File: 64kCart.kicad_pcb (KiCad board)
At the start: 2 copper layers, 9 parts, among them SW1 SW_Push, U1 27C512, U2 74LS173, U3 74LS04, U4 C64-Exp-Port

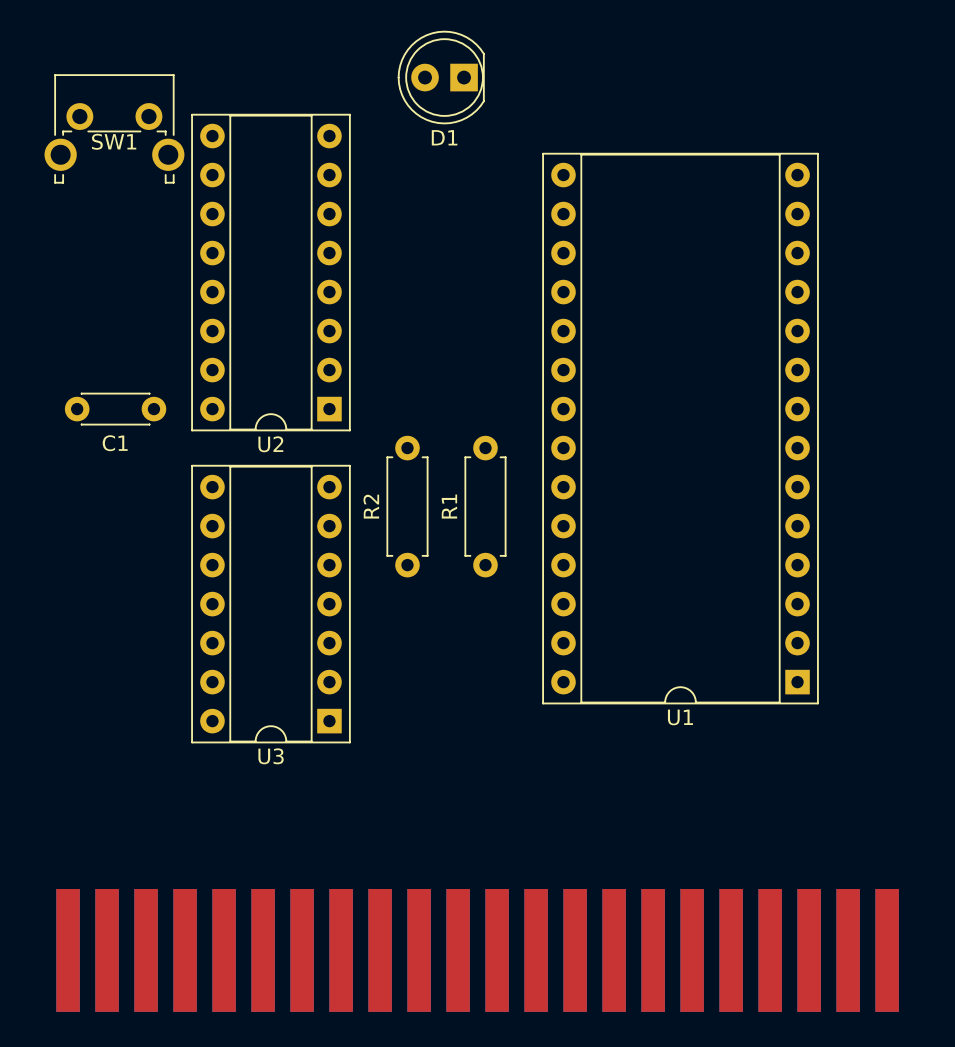
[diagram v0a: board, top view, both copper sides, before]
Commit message: Some work on board layout.
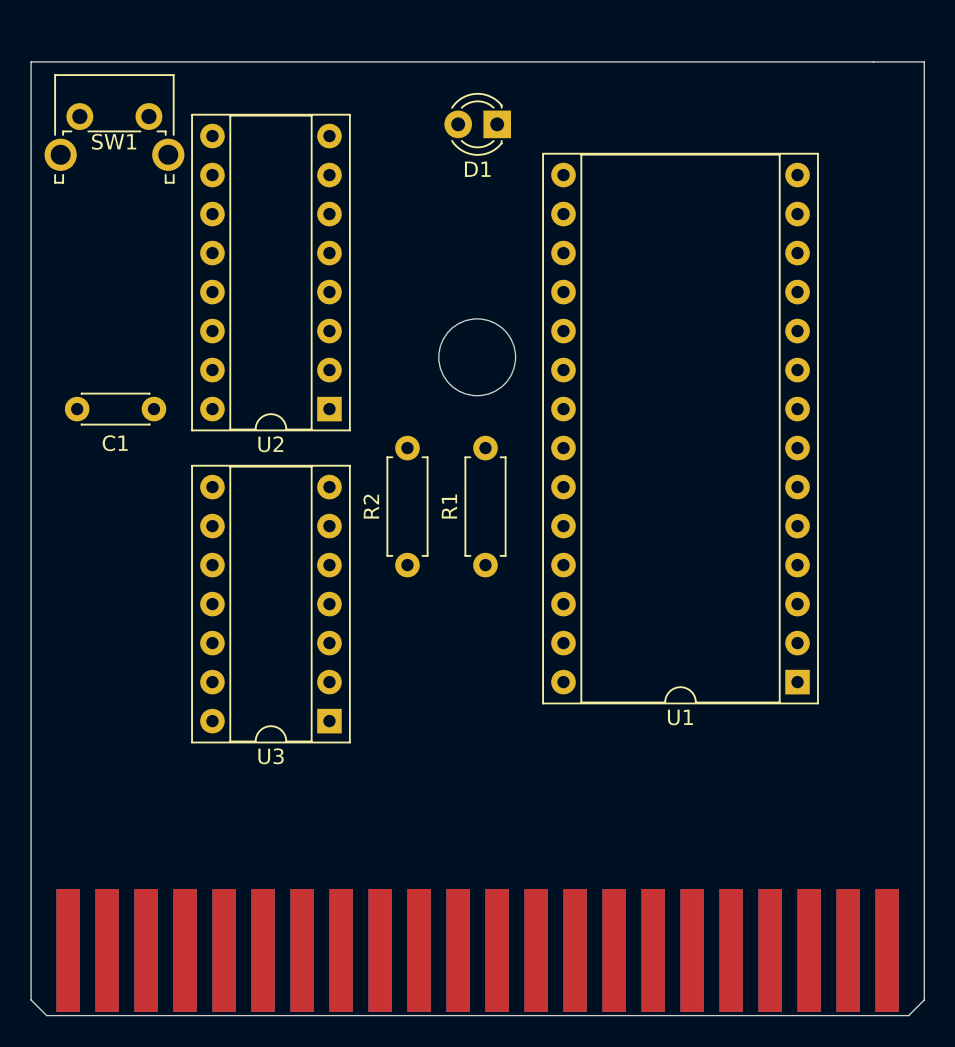
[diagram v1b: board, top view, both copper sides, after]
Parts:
- added H1: MountingHole, Mounting_Holes:MountingHole_5mm, F.Cu at (136.9, 95.9)
- D1: footprint LEDs:LED_D5.0mm -> LEDs:LED_D3.0mm
- moved D1 3.74 mm to (138.2, 80.8)
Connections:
- net Net-(U2-Pad10) renamed /IO1
- net Net-(U2-Pad6) renamed /EXROM
- U4 pad 10: (no net) -> Net-(U4-Pad10)
- U4 pad 12: (no net) -> Net-(U4-Pad12)
- U4 pad 13: (no net) -> Net-(U4-Pad13)
- U4 pad 4: (no net) -> Net-(U4-Pad4)
- U4 pad 5: (no net) -> Net-(U4-Pad5)
- U4 pad 6: (no net) -> Net-(U4-Pad6)
- U4 pad 8: (no net) -> Net-(U4-Pad8)
- U4 pad B: (no net) -> Net-(U4-PadB)
- U4 pad D: (no net) -> Net-(U4-PadD)
- U4 pad F: (no net) -> Net-(U4-PadF)
- U4 pad H: (no net) -> Net-(U4-PadH)
- U4 pad J: (no net) -> Net-(U4-PadJ)
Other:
- board outline added: 58.2 x 62.1 mm

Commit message: First layout completed.
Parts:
- added G***: LOGO, Logo:bigby2, F.Cu at (118.7, 126.0)
- H1: footprint Mounting_Holes:MountingHole_5mm -> 64kCart:MountingHole_CartCombined
- SW1: value SW_Push -> Reset
- moved C1 21.5 mm to (112.9, 120.7), turned to 0 degrees
- moved U2 19.2 mm to (119.1, 116.7)
- moved D1 19.2 mm to (123.1, 92.6), turned to 0 degrees
- moved SW1 11.7 mm to (113.5, 91.7)
- moved U3 8.42 mm to (134.2, 124.3)
- moved U1 7.49 mm to (159.6, 124.3)
- moved R1 7.49 mm to (139.3, 116.7)
- moved R2 6.60 mm to (126.6, 106.2)
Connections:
- U4 pad 10: Net-(U4-Pad10) -> (no net)
- U4 pad 12: Net-(U4-Pad12) -> (no net)
- U4 pad 13: Net-(U4-Pad13) -> (no net)
- U4 pad 4: Net-(U4-Pad4) -> (no net)
- U4 pad 5: Net-(U4-Pad5) -> (no net)
- U4 pad 6: Net-(U4-Pad6) -> (no net)
- U4 pad 8: Net-(U4-Pad8) -> (no net)
- U4 pad B: Net-(U4-PadB) -> (no net)
- U4 pad D: Net-(U4-PadD) -> (no net)
- U4 pad F: Net-(U4-PadF) -> (no net)
- U4 pad H: Net-(U4-PadH) -> (no net)
- U4 pad J: Net-(U4-PadJ) -> (no net)
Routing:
- net GND: track 0.00 -> 289.6 mm, vias 0 -> 6
- net +5V: track 0.00 -> 118.6 mm, vias 0 -> 5
- net /D1: track 0.00 -> 105.9 mm, vias 0 -> 1
- net /D2: track 0.00 -> 100.3 mm, vias 0 -> 2
- net /D3: track 0.00 -> 92.8 mm, vias 0 -> 1
- net /D0: track 0.00 -> 89.5 mm, vias 0 -> 1
- net /RESET: track 0.00 -> 61.1 mm, vias 0 -> 1
- net /EXROM: track 0.00 -> 45.0 mm
- net /A12: track 0.00 -> 44.9 mm, vias 0 -> 2
- net /ROML: track 0.00 -> 44.4 mm, vias 0 -> 1
- net /D4: track 0.00 -> 44.1 mm
- net /D5: track 0.00 -> 40.5 mm
- net /IO1: track 0.00 -> 38.9 mm
- net /D6: track 0.00 -> 38.3 mm
- net /A0: track 0.00 -> 36.4 mm
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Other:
- board size 58.2 x 62.1 mm -> 58.2 x 49.9 mm
- net class Power: trace_width 0.4 -> 0.5
- board text added: "2019 Rev.1"
- board text added: "64kCart Remix"
- board text added: "64kCart Remix 2019 Rev.1 - https://www.hackup.net Based on the original "64k Karte" design by Hucky."
